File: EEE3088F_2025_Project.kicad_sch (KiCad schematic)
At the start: 44 parts, among them J1 Conn_02x16_Odd_Even, J2 USB_C_Receptacle_PowerOnly_6P, J3 Conn_01x02, Q1 PNP, SW1 SW_SPST, U1 HR8833, U2 HR8833, U3 MIC2026-1YM, U4 HT7533-1, U5 TPS613222ADBV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

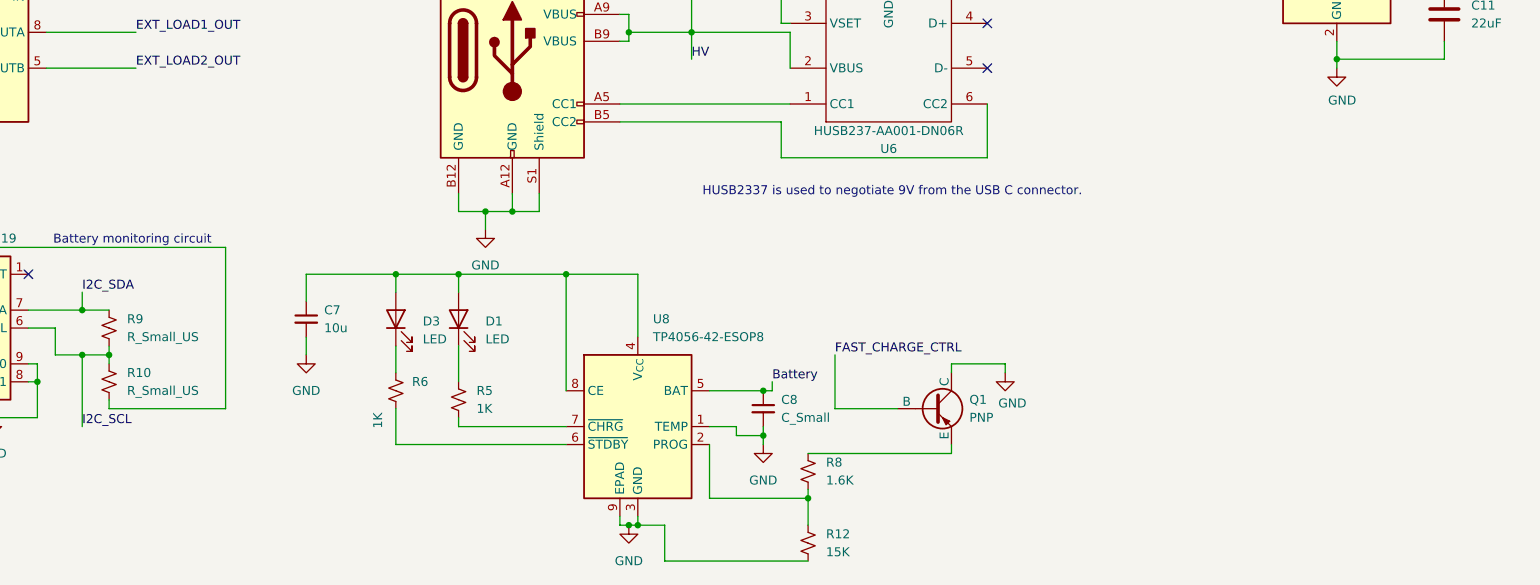
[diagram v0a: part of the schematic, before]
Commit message: Added new footprint for 1*2 connector
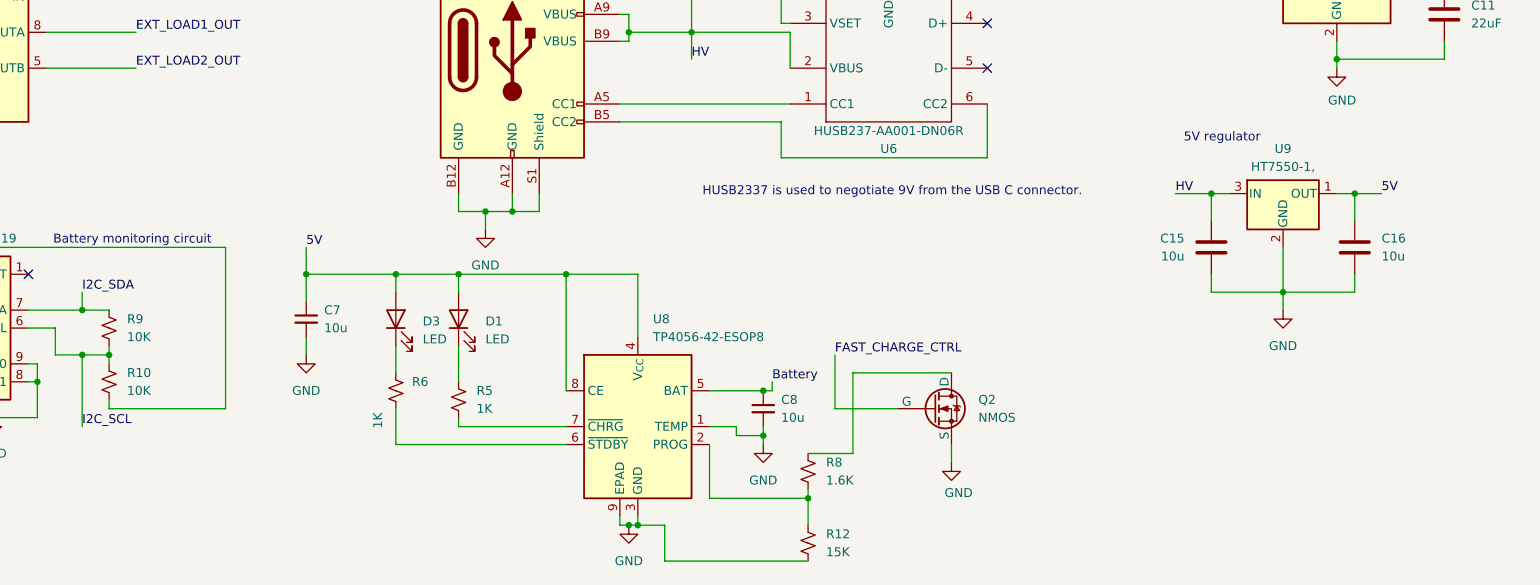
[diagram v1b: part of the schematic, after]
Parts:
- removed Q1: PNP, symbol Simulation_SPICE:PNP
- added C15, C16: 10u, Capacitor_SMD:C_0805_2012Metric_Pad1.18x1.45mm_HandSolder, symbol Device:C
- added Q2: NMOS, Package_TO_SOT_SMD:Infineon_PG-HSOF-8-1, symbol Simulation_SPICE:NMOS
- added U9: HT7550-1,, Package_TO_SOT_SMD:SOT-89-3, symbol Regulator_Linear:L78L33_SOT89
- C11, C12, C2, C3, C4, C6: footprint Capacitor_SMD:C_0201_0603Metric -> Capacitor_SMD:C_0805_2012Metric_Pad1.18x1.45mm_HandSolder
- C13, C7: footprint Capacitor_SMD:C_0201_0603Metric_Pad0.64x0.40mm_HandSolder -> Capacitor_SMD:C_0805_2012Metric_Pad1.18x1.45mm_HandSolder
- C14: footprint (none) -> Capacitor_SMD:C_0805_2012Metric_Pad1.18x1.45mm_HandSolder
- C8: value C_Small -> 10u; footprint (none) -> Capacitor_SMD:C_0805_2012Metric_Pad1.18x1.45mm_HandSolder
- J3: footprint Connector_PinHeader_2.54mm:PinHeader_1x02_P2.54mm_Vertical -> Connector_JST:JST_PH_S2B-PH-K_1x02_P2.00mm_Horizontal
- R10, R9: value R_Small_US -> 10K
- R13: LCSC (none) -> C5375459
- U3: LCSC (none) -> C144190
- U7: LCSC (none) -> C87469
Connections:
- net FAST_CHARGE_CTRL: now also Q2.2 (G)
- net GND: now also C15.2, C16.2, Q2.3 (S), U9.2 (GND)
- net HV: now also C15.1, U9.3 (IN)
- net 5V: now reaches C7.1, D1.2 (A), D3.2 (A), U8.4 (V_{CC}), U8.8 (CE)
- net 5V: now also C16.1, U9.1 (OUT)
- net at R8.1: now also Q2.1 (D)
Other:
- note added: "5V regulator"

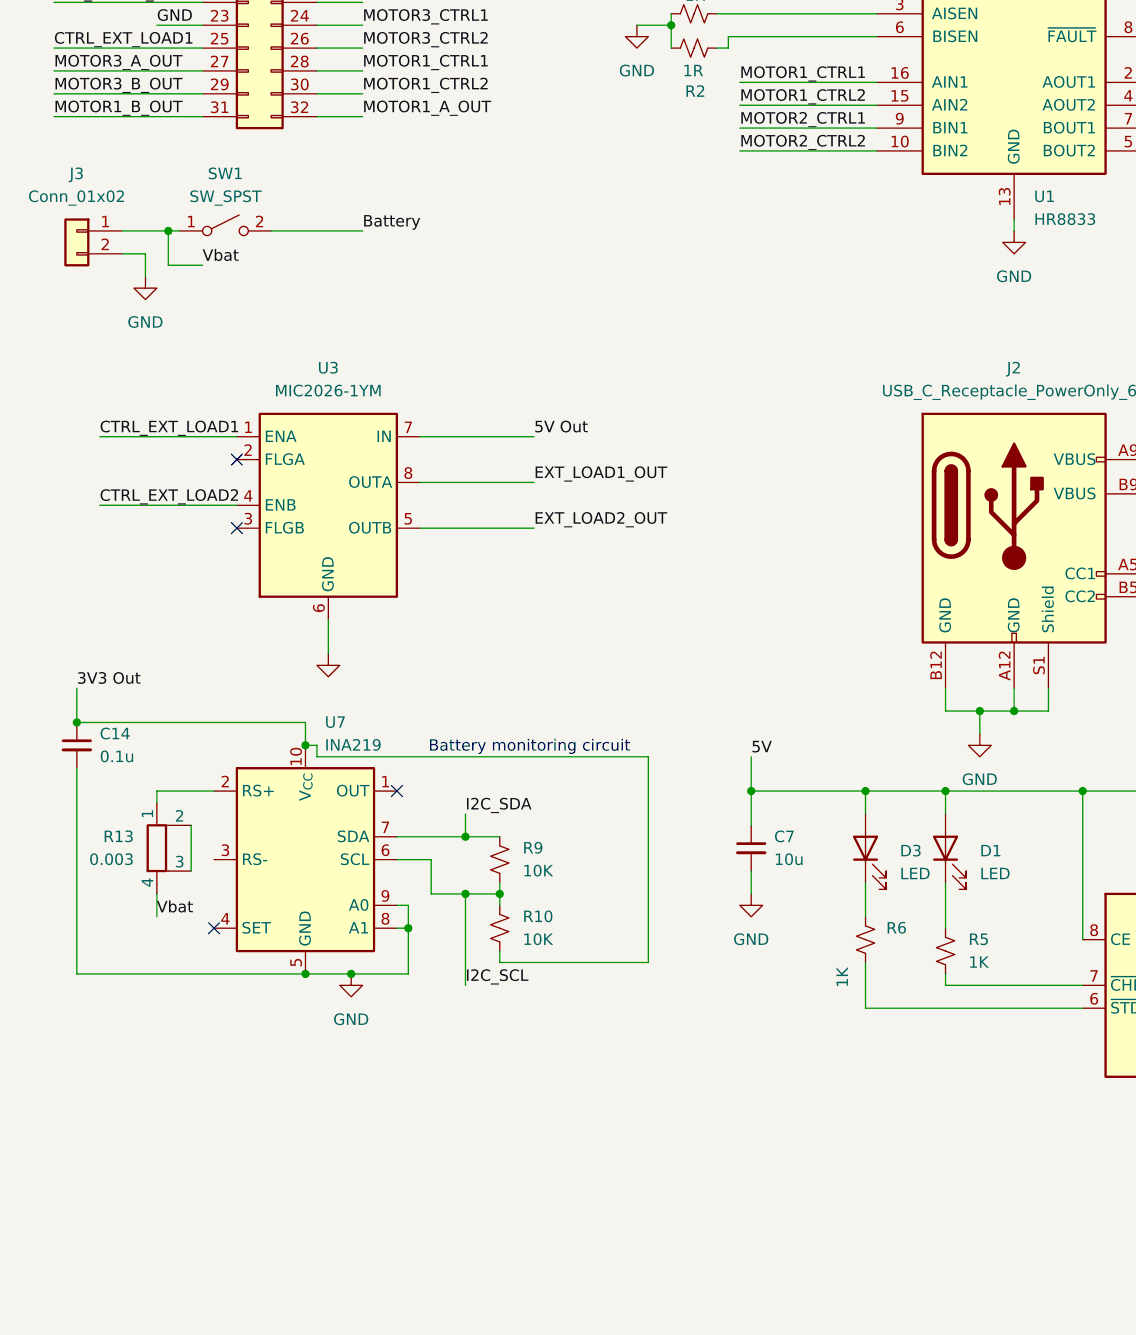
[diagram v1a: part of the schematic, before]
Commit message: Changed the configuration for INA219
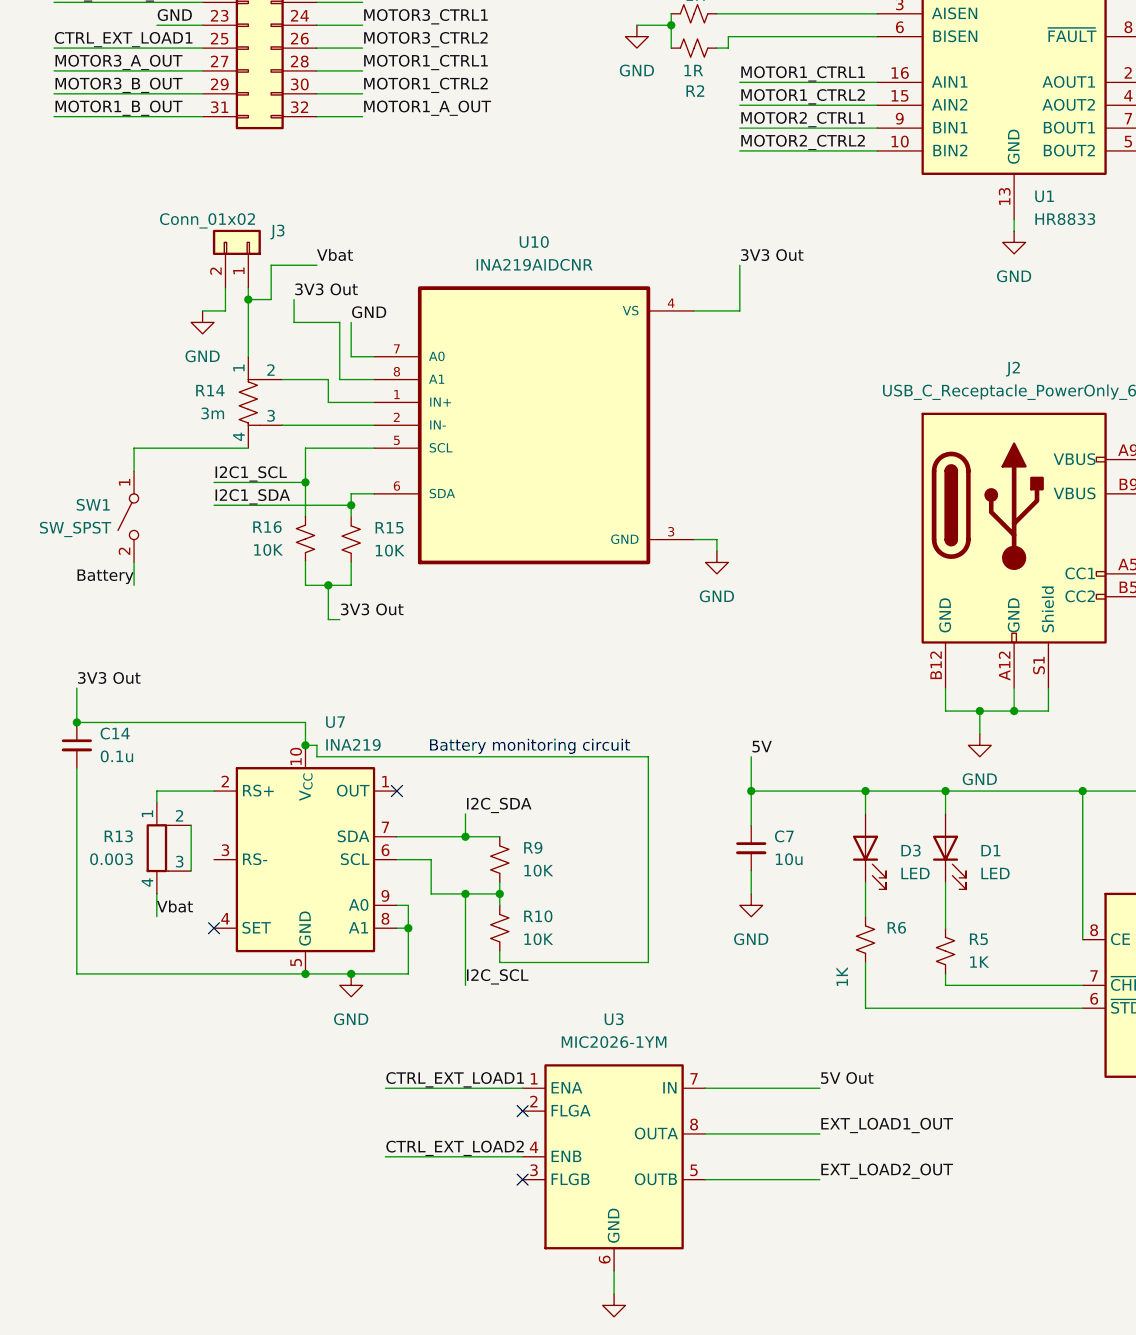
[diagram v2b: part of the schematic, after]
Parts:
- added R14: 3m, symbol Device:R_Shunt_US
- added R15, R16: 10K, symbol Device:R_Small_US
- added U10: INA219AIDCNR, Package_TO_SOT_SMD:SOT-23-8_Handsoldering, symbol INA219AIDCNR:INA219AIDCNR
- U7: footprint Package_SO:MSOP-10_3x3mm_P0.5mm -> Package_TO_SOT_SMD:SOT-23-8_Handsoldering
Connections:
- net 3V3 Out: now also R15.2, R16.2, U10.4 (VS), U10.8 (A1)
- net GND: now also U10.3 (GND), U10.7 (A0)
- net I2C1_SCL: now also R16.1, U10.5 (SCL)
- net I2C1_SDA: now also R15.1, U10.6 (SDA)
- net Vbat: now also R14.1; no longer SW1.1 (A)
- new net: R14.2, U10.1 (IN+)
- new net: R14.3, U10.2 (IN-)
- new net: R14.4, SW1.1 (A)
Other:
- moved on the sheet: J3, SW1, U3

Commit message: Added LCSC numbers and changed switch to SPDT
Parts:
- removed C14: 0.1u, Capacitor_SMD:C_0805_2012Metric_Pad1.18x1.45mm_HandSolder, symbol Device:C_Small
- removed R10, R9: 10K, Resistor_SMD:R_0201_0603Metric_Pad0.64x0.40mm_HandSolder, symbol Device:R_Small_US
- removed R13: 0.003, Resistor_SMD:R_Shunt_Vishay_WSK2512_6332Metric_T1.19mm, symbol Device:R_Shunt
- removed SW1: SW_SPST, Button_Switch_THT:SW_Tactile_SPST_Angled_PTS645Vx83-2LFS, symbol Switch:SW_SPST
- removed U7: INA219, Package_TO_SOT_SMD:SOT-23-8_Handsoldering, symbol Power_Management:MAX9612
- added SW1: SW_SPDT, Button_Switch_THT:SW_Slide_SPDT_Angled_CK_OS102011MA1Q, symbol Switch:SW_SPDT
- C13: LCSC (none) -> C18438
- C3, C4: LCSC 1710 -> C1710
- J1, J3: now left out of the parts list
- R14: footprint (none) -> Resistor_SMD:R_Shunt_Vishay_WSR2_WSR3_KelvinConnection; LCSC (none) -> C5375459
- R15, R16: footprint (none) -> Resistor_SMD:R_1206_3216Metric_Pad1.30x1.75mm_HandSolder
- R8: LCSC (none) -> C17394
- U10: LCSC (none) -> C87469
- U8: LCSC (none) -> C16581
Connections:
- net Battery: now also SW1.1 (A); no longer C8.1, U8.5 (BAT)
- net Vbat: now also C8.1, U8.5 (BAT)
- net at R14.4: now also SW1.2 (B)
- no-connect marks 9 -> 7
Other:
- note removed: "Battery monitoring circuit"
- moved on the sheet: J3, R14, R15, R16, U10

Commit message: fixed footprint for SW1 to be vertical pin
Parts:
- SW1: LCSC C431541 -> C92656
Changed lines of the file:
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@@
 			)
 		)
-		(property "LCSC" "C431541"
+		(property "LCSC" "C92656"
 			(at 24.13 119.38 90)
 			(effects

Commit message: Changed regulator and NMOS footprint
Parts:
- C15: value 10u -> 0.33u; footprint Capacitor_SMD:C_0805_2012Metric_Pad1.18x1.45mm_HandSolder -> Capacitor_SMD:C_0201_0603Metric_Pad0.64x0.40mm_HandSolder; LCSC (none) -> C5139492
- C16: footprint Capacitor_SMD:C_0805_2012Metric_Pad1.18x1.45mm_HandSolder -> Capacitor_SMD:C_0201_0603Metric_Pad0.64x0.40mm_HandSolder; LCSC (none) -> C3011652
- Q2: footprint Package_TO_SOT_SMD:Infineon_PG-HSOF-8-1 -> Package_TO_SOT_SMD:SOT-23-3; LCSC (none) -> C20917
- U9: value HT7550-1, -> CJ78L05; LCSC C14289 -> C2079
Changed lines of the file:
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@@
 			)
 		)
-		(property "Footprint" "Capacitor_SMD:C_0805_2012Metric_Pad1.18x1.45mm_HandSolder"
+		(property "Footprint" "Capacitor_SMD:C_0201_0603Metric_Pad0.64x0.40mm_HandSolder"
 			(at 243.5352 135.89 0)
 			(effects
@@
 		)
 		(property "Description" "Unpolarized capacitor"
+			(at 242.57 132.08 0)
+			(effects
+				(font
+					(size 1.27 1.27)
+				)
+				(hide yes)
+			)
+		)
+		(property "LCSC" "C3011652"
 			(at 242.57 132.08 0)
 			(effects
@@
 			)
 		)
-		(property "Footprint" "Package_TO_SOT_SMD:Infineon_PG-HSOF-8-1"
+		(property "Footprint" "Package_TO_SOT_SMD:SOT-23-3"
 			(at 187.96 152.4 0)
 			(effects
@@
 		(property "Sim.Pins" "1=D 2=G 3=S"
 			(at 182.88 170.18 0)
+			(effects
+				(font
+					(size 1.27 1.27)
+				)
+				(hide yes)
+			)
+		)
+		(property "LCSC" "C20917"
+			(at 182.88 154.94 0)
 			(effects
 				(font
@@
 			)
 		)
-		(property "Value" "HT7550-1,"
+		(property "Value" "CJ78L05"
 			(at 232.41 120.65 0)
 			(effects
@@
 			)
 		)
-		(property "Datasheet" "https://jlcpcb.com/api/file/downloadByFileSystemAccessId/8579707787284303872"
+		(property "Datasheet" "https://jlcpcb.com/api/file/downloadByFileSystemAccessId/8579710244295413760"
 			(at 232.41 125.73 0)
 			(effects
@@
 			)
 		)
-		(property "Description" "100mA Fixed 3.3V Positive electrode 30V SOT-89-3 Voltage Regulators - Linear, Low Drop Out (LDO) Regulators ROHS"
+		(property "Description" "100mA Fixed 5V Positive electrode 30V SOT-89-3L Voltage Regulators - Linear, Low Drop Out (LDO) Regulators ROHS"
 			(at 232.41 124.46 0)
 			(effects
@@
 			)
 		)
-		(property "LCSC" "C14289"
+		(property "LCSC" "C2079"
 			(at 232.41 124.46 0)
 			(effects
@@
 		(exclude_from_sim no)
 		(in_bom no)
-		(on_board no)
+		(on_board yes)
 		(dnp no)
 		(fields_autoplaced yes)
@@
 		(exclude_from_sim no)
 		(in_bom no)
-		(on_board no)
+		(on_board yes)
 		(dnp no)
 		(property "Reference" "J3"
@@
 			)
 		)
-		(property "Value" "10u"
+		(property "Value" "0.33u"
 			(at 218.44 133.3499 0)
 			(effects
@@
 			)
 		)
-		(property "Footprint" "Capacitor_SMD:C_0805_2012Metric_Pad1.18x1.45mm_HandSolder"
+		(property "Footprint" "Capacitor_SMD:C_0201_0603Metric_Pad0.64x0.40mm_HandSolder"
 			(at 221.2848 135.89 0)
 			(effects
@@
 			(at 222.25 132.08 0)
 			(effects
+				(font
+					(size 1.27 1.27)
+				)
+				(hide yes)
+			)
+		)
+		(property "LCSC" "C5139492"
+			(at 222.25 132.08 0)
+			(effects

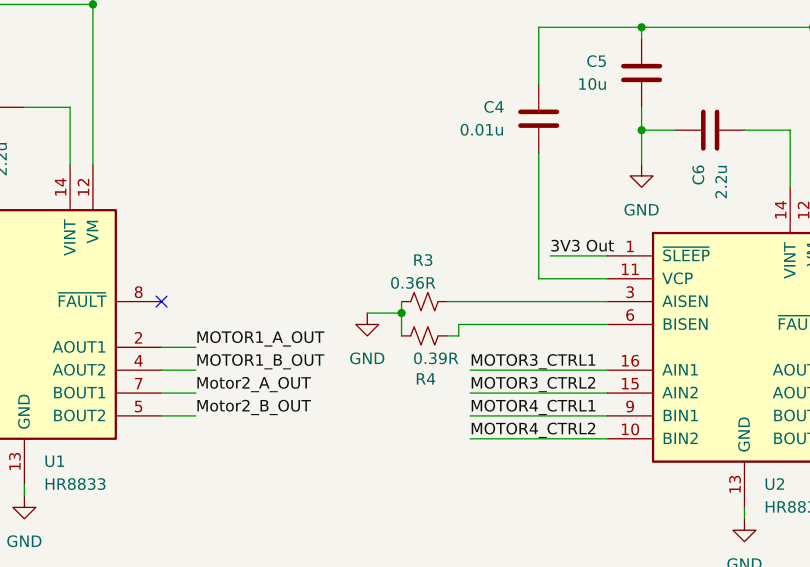
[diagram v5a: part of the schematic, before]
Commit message: Added edge cuts
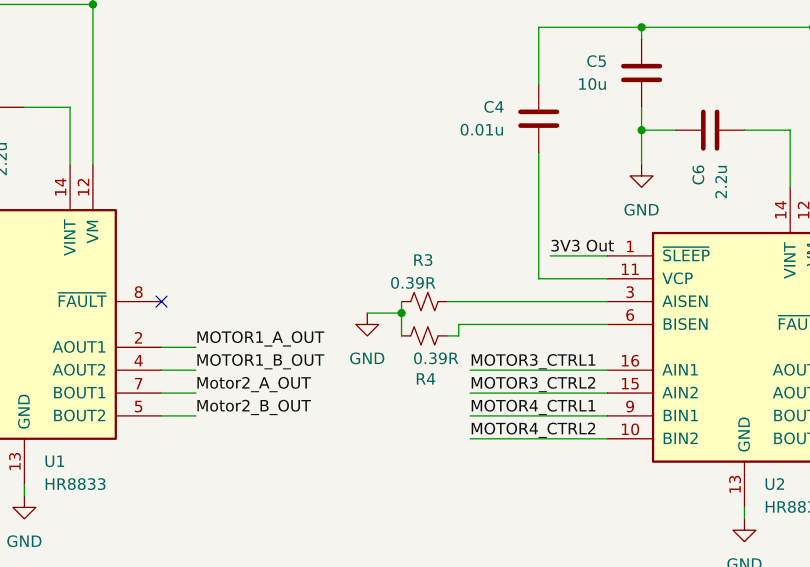
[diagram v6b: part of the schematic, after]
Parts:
- R14: footprint Resistor_SMD:R_Shunt_Vishay_WSR2_WSR3_KelvinConnection -> Resistor_SMD:R_Shunt_Vishay_WSK2512_6332Metric_T2.21mm
- R3: value 0.36R -> 0.39R
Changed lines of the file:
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@@
 			)
 		)
-		(property "Footprint" "Resistor_SMD:R_Shunt_Vishay_WSR2_WSR3_KelvinConnection"
+		(property "Footprint" "Resistor_SMD:R_Shunt_Vishay_WSK2512_6332Metric_T2.21mm"
 			(at 35.052 106.68 90)
 			(effects
@@
 			)
 		)
-		(property "Value" "0.36R"
+		(property "Value" "0.39R"
 			(at 168.91 50.038 90)
 			(effects
